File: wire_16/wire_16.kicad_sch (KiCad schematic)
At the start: 2 parts, among them J1 Moat_Wire_16, J2 Moat_Wire_12

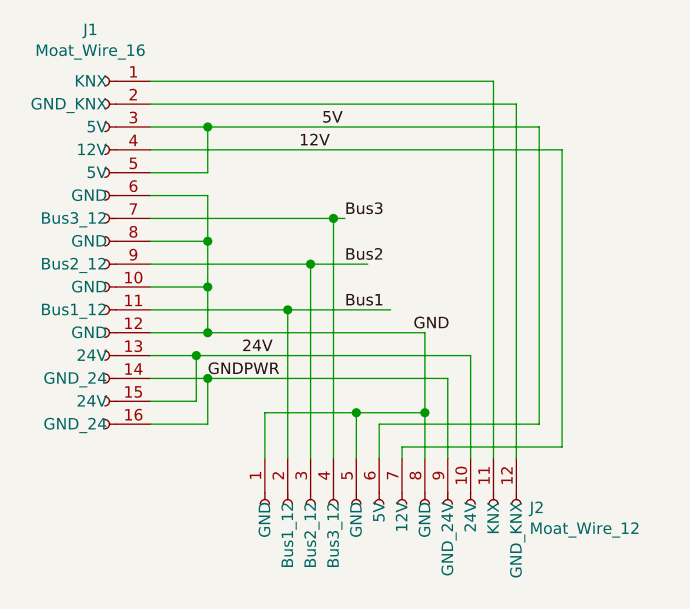
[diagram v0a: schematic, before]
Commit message: Plug updates
drop in/out from plug24
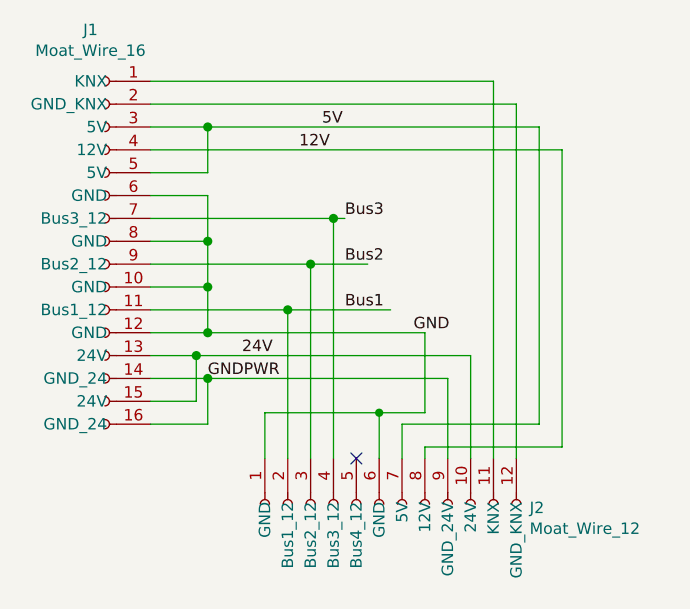
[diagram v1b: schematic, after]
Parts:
- J2: symbol local:Moat_Wire_12 -> localstuff:Moat_Wire_12
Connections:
- net 12V: now also J2.8 (12V); no longer J2.7 (12V)
- net 5V: now also J2.7 (5V); no longer J2.6 (5V)
- net GND: now also J2.6 (GND); no longer J2.5 (GND), J2.8 (GND)
- no-connect marks 0 -> 1
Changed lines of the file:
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@@
 (kicad_sch (version 20211123) (generator eeschema)
   (paper "A4")
-  (junction (at 45.72 57.15) (diameter 1.016) (color 0 0 0 0)
-  )
   (junction (at 29.21 43.18) (diameter 1.016) (color 0 0 0 0)
   )
@@
   (junction (at 29.21 38.1) (diameter 1.016) (color 0 0 0 0)
   )
-  (junction (at 53.34 57.15) (diameter 1.016) (color 0 0 0 0)
-  )
   (junction (at 40.64 40.64) (diameter 1.016) (color 0 0 0 0)
   )
@@
   (junction (at 38.1 45.72) (diameter 1.016) (color 0 0 0 0)
   )
+  (junction (at 48.26 57.15) (diameter 0) (color 0 0 0 0)
+  )
   (junction (at 43.18 35.56) (diameter 1.016) (color 0 0 0 0)
   )
@@
   (junction (at 29.21 48.26) (diameter 1.016) (color 0 0 0 0)
   )
+  (no_connect (at 45.72 62.23))
   (wire (pts (xy 29.21 25.4) (xy 66.04 25.4))
     (stroke (width 0) (type solid) (color 0 0 0 0))
@@
     (stroke (width 0) (type solid) (color 0 0 0 0))
   )
+  (wire (pts (xy 48.26 57.15) (xy 48.26 62.23))
+    (stroke (width 0) (type default) (color 0 0 0 0))
+  )
   (wire (pts (xy 22.86 55.88) (xy 27.94 55.88))
     (stroke (width 0) (type solid) (color 0 0 0 0))
@@
     (stroke (width 0) (type solid) (color 0 0 0 0))
   )
-  (wire (pts (xy 35.56 57.15) (xy 45.72 57.15))
+  (wire (pts (xy 35.56 57.15) (xy 48.26 57.15))
     (stroke (width 0) (type solid) (color 0 0 0 0))
   )
@@
     (stroke (width 0) (type solid) (color 0 0 0 0))
   )
-  (wire (pts (xy 68.58 60.96) (xy 50.8 60.96))
-    (stroke (width 0) (type solid) (color 0 0 0 0))
-  )
-  (wire (pts (xy 48.26 62.23) (xy 48.26 58.42))
-    (stroke (width 0) (type solid) (color 0 0 0 0))
-  )
-  (wire (pts (xy 53.34 62.23) (xy 53.34 57.15))
-    (stroke (width 0) (type solid) (color 0 0 0 0))
-  )
-  (wire (pts (xy 45.72 62.23) (xy 45.72 57.15))
-    (stroke (width 0) (type solid) (color 0 0 0 0))
+  (wire (pts (xy 53.34 62.23) (xy 53.34 60.96))
+    (stroke (width 0) (type default) (color 0 0 0 0))
   )
   (wire (pts (xy 38.1 62.23) (xy 38.1 45.72))
@@
     (stroke (width 0) (type solid) (color 0 0 0 0))
   )
+  (wire (pts (xy 48.26 57.15) (xy 53.34 57.15))
+    (stroke (width 0) (type solid) (color 0 0 0 0))
+  )
   (wire (pts (xy 49.53 45.72) (xy 38.1 45.72))
     (stroke (width 0) (type solid) (color 0 0 0 0))
@@
     (stroke (width 0) (type solid) (color 0 0 0 0))
   )
-  (wire (pts (xy 50.8 60.96) (xy 50.8 62.23))
-    (stroke (width 0) (type solid) (color 0 0 0 0))
-  )
   (wire (pts (xy 29.21 53.34) (xy 55.88 53.34))
     (stroke (width 0) (type solid) (color 0 0 0 0))
@@
     (stroke (width 0) (type solid) (color 0 0 0 0))
   )
-  (wire (pts (xy 48.26 58.42) (xy 66.04 58.42))
-    (stroke (width 0) (type solid) (color 0 0 0 0))
-  )
   (wire (pts (xy 27.94 50.8) (xy 22.86 50.8))
     (stroke (width 0) (type solid) (color 0 0 0 0))
   )
-  (wire (pts (xy 45.72 57.15) (xy 53.34 57.15))
-    (stroke (width 0) (type solid) (color 0 0 0 0))
-  )
   (wire (pts (xy 27.94 50.8) (xy 58.42 50.8))
     (stroke (width 0) (type solid) (color 0 0 0 0))
@@
     (stroke (width 0) (type solid) (color 0 0 0 0))
   )
+  (wire (pts (xy 53.34 60.96) (xy 68.58 60.96))
+    (stroke (width 0) (type default) (color 0 0 0 0))
+  )
   (wire (pts (xy 29.21 38.1) (xy 29.21 33.02))
     (stroke (width 0) (type solid) (color 0 0 0 0))
@@
   (wire (pts (xy 29.21 25.4) (xy 29.21 30.48))
     (stroke (width 0) (type solid) (color 0 0 0 0))
+  )
+  (wire (pts (xy 50.8 58.42) (xy 50.8 62.23))
+    (stroke (width 0) (type default) (color 0 0 0 0))
+  )
+  (wire (pts (xy 66.04 58.42) (xy 50.8 58.42))
+    (stroke (width 0) (type default) (color 0 0 0 0))
   )
   (wire (pts (xy 40.64 40.64) (xy 22.86 40.64))
@@
     (pin "9")
   )
-  (symbol (lib_id "local:Moat_Wire_12") (at 58.42 67.31 90) (mirror x) (unit 1)
+  (symbol (lib_id "localstuff:Moat_Wire_12") (at 58.42 67.31 90) (mirror x) (unit 1)
     (in_bom yes) (on_board yes)
     (property "Reference" "J2" (id 0) (at 64.9732 67.7164 90)
